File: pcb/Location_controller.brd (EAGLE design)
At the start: 75 x 45 mm, 41 parts, among them IC1 LIS302DL, X1 22-23-2021

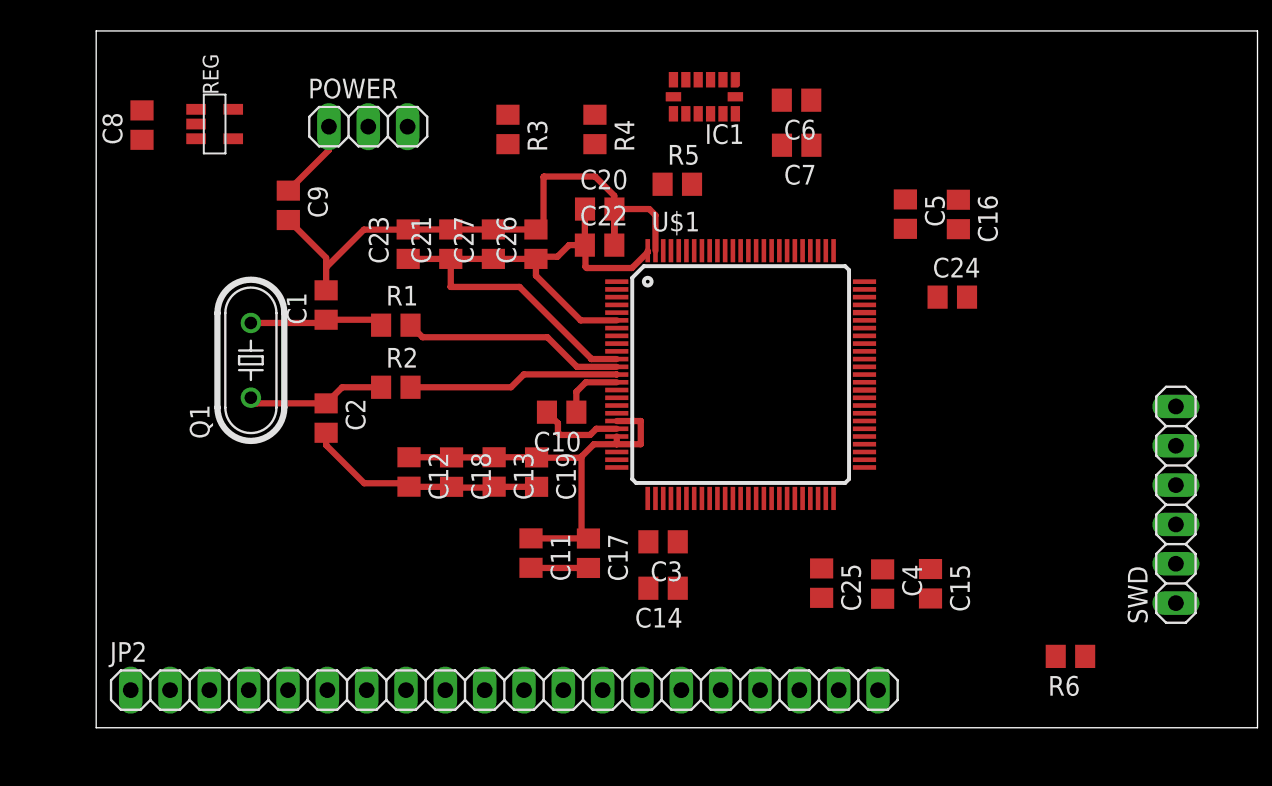
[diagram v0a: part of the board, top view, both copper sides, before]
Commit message: Add more layering
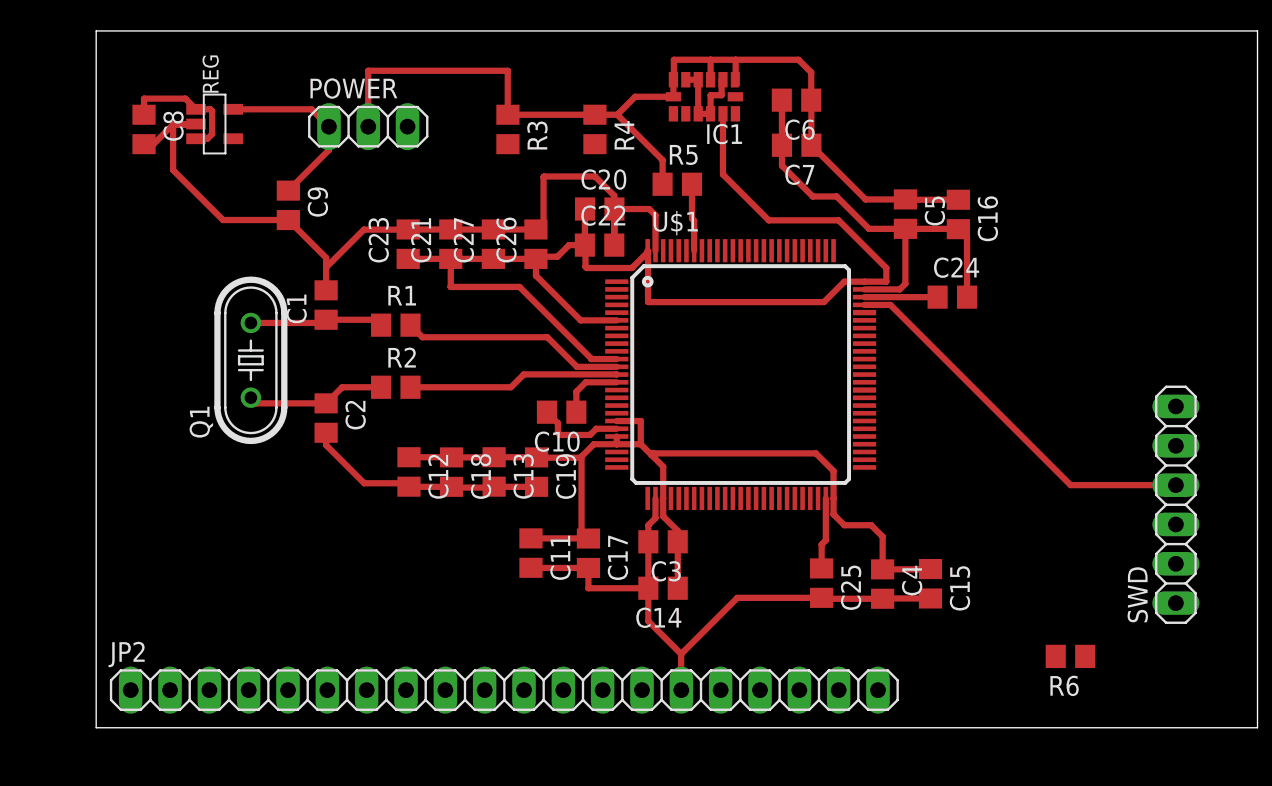
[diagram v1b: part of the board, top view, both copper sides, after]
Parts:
- moved C8 0.31 mm to (3.09, 38.6), turned to 270 degrees
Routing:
- net VDD: track 70.5 -> 204.2 mm
- net GND: track 64.4 -> 152.9 mm
- net SWDIO: track 0.00 -> 24.9 mm
- net N$4: track 0.00 -> 8.43 mm
- net N$10: track 5.22 -> 11.9 mm
- net N$9: track 0.00 -> 4.72 mm
- net N$8: track 0.00 -> 4.63 mm
- net N$3: track 0.00 -> 4.35 mm

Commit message: Further pcb layout routing
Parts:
- added DRN_POWER, RCM_POWER: (no value), pinhead:1X02
- moved C8 52.6 mm to (55.7, 37.7), turned to 90 degrees
- moved C9 52.3 mm to (64.5, 38.7), turned to 0 degrees
- moved REG 51.9 mm to (59.8, 37.8)
- moved POWER 34.4 mm to (51.9, 41.4)
- moved SWD 4.65 mm to (70.7, 9.85)
- moved R6 1.90 mm to (64.8, 4.26)
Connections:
- removed net N$10: C9.1, POWER.1, REG.5
- new net IN_3V: C8.1, POWER.2, REG.1, REG.3
- new net N$5: POWER.1, X1.1
- net GND: now also DRN_POWER.1, RCM_POWER.1
- net N$4: now also DRN_POWER.2, POWER.3; no longer C8.1, REG.1, REG.3, X1.1
- net VDD: now also C9.1, REG.5; no longer POWER.2
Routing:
- net GND: track 152.9 -> 231.7 mm
- net N$4: track 8.43 -> 55.2 mm
- net NRST: track 4.18 -> 44.9 mm, vias 0 -> 2
- net SWO: track 0.00 -> 39.3 mm, vias 0 -> 1
- net SWCLK: track 0.00 -> 37.0 mm, vias 0 -> 1
- net USART2_TX: track 0.00 -> 22.8 mm, vias 0 -> 1
- net USART2_RX: track 0.00 -> 21.3 mm, vias 0 -> 1
- net IN_3V: track 0.00 -> 15.0 mm
- net SWDIO: track 24.9 -> 39.8 mm
- net VDD: track 204.2 -> 216.7 mm
- net N$10: track 11.9 -> 0.00 mm
- net N$6: track 0.00 -> 5.28 mm

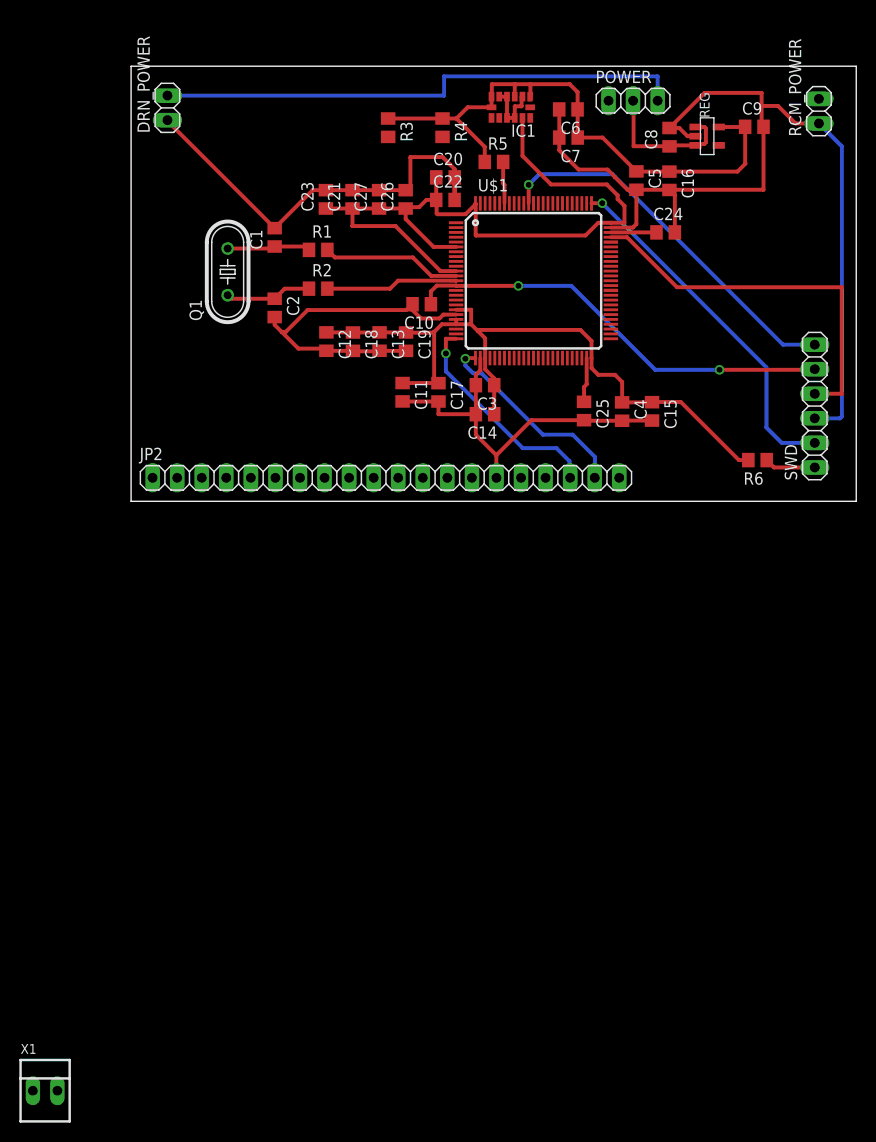
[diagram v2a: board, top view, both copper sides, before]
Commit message: Add barrel DC-jack to pcb
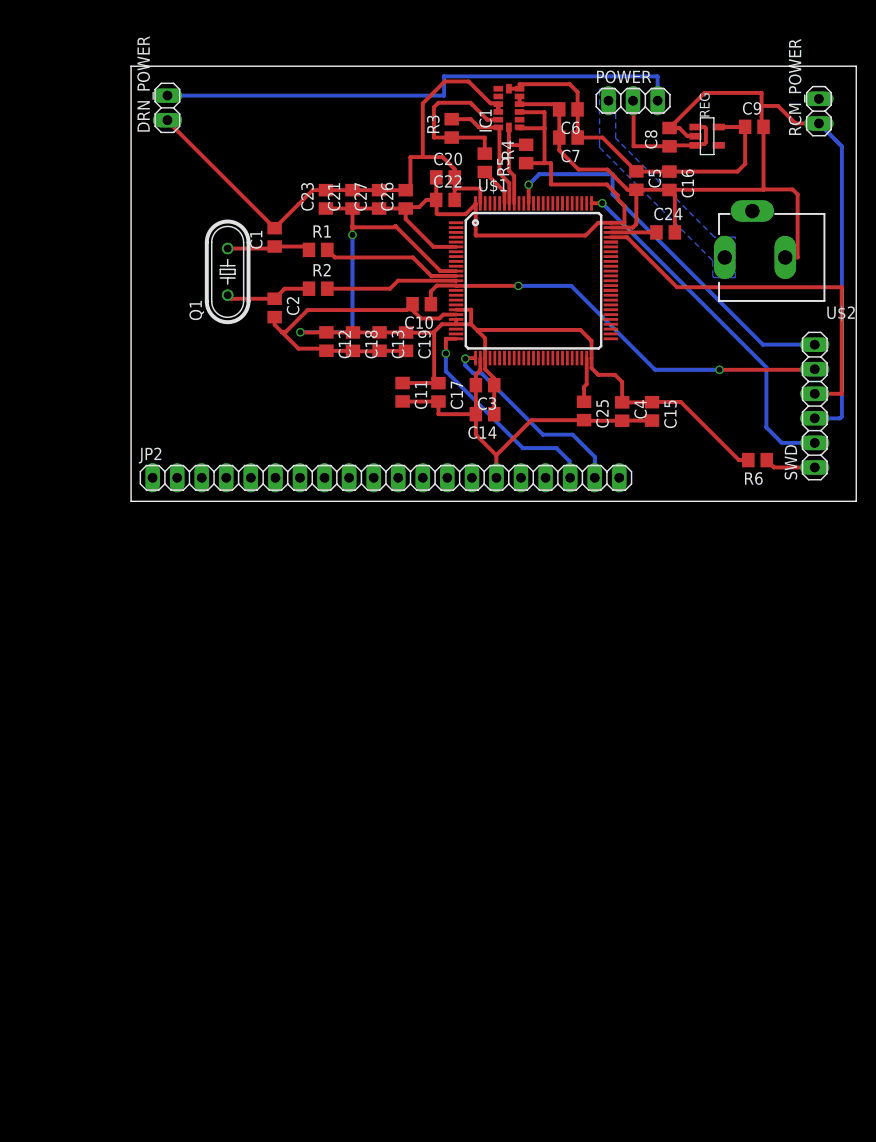
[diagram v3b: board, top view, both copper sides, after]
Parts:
- removed X1: 22-23-2021, con-molex:22-23-2021
- added U$2: DCBARRELPTH, BaseApp:DCJACK_2MM_PTH
- moved R4 9.07 mm to (40.9, 35.9), turned to 90 degrees
- moved R3 6.57 mm to (33.2, 38.6), turned to 90 degrees
- moved R5 0.95 mm to (36.6, 35.0), turned to 270 degrees
- moved IC1 0.22 mm to (39.1, 40.7), turned to 90 degrees
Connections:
- new net GNDBREAK: U$2.GNDBREAK
- net GND: now also U$2.GND; no longer X1.2
- net N$5: now also U$2.PWR; no longer X1.1
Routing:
- net GND: track 231.7 -> 260.7 mm
- net VDD: track 216.7 -> 237.5 mm, vias 0 -> 2
- net I2C_SDA: track 0.00 -> 13.5 mm
- net I2C_SCL: track 0.00 -> 9.89 mm
- net SWO: track 39.3 -> 40.5 mm
- added copper zone on layer 16, net N$5

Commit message: Finish pcb routing
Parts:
- added JP1, JP3: (no value), pinhead:1X06
- JP2: device pinhead:1X20 -> pinhead:1X06
- moved JP2 0.97 mm to (25.4, 2.54)
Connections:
- net GND: now also JP1.1; no longer JP2.15
- net IN_3V: now also RCM_POWER.2
- net USART2_RX: now also JP1.5; no longer JP2.19
- net USART2_TX: now also JP1.4; no longer JP2.18
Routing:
- net GND: track 260.7 -> 324.7 mm, vias 0 -> 6
- net VDD: track 237.5 -> 272.8 mm, vias 2 -> 5
- net IN_3V: track 15.0 -> 39.4 mm
- net N$4: track 55.2 -> 59.9 mm
- net USART2_TX: track 22.8 -> 20.9 mm
- net SWCLK: track 37.0 -> 38.2 mm
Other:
- board size 75 x 45 mm -> 75 x 48 mm

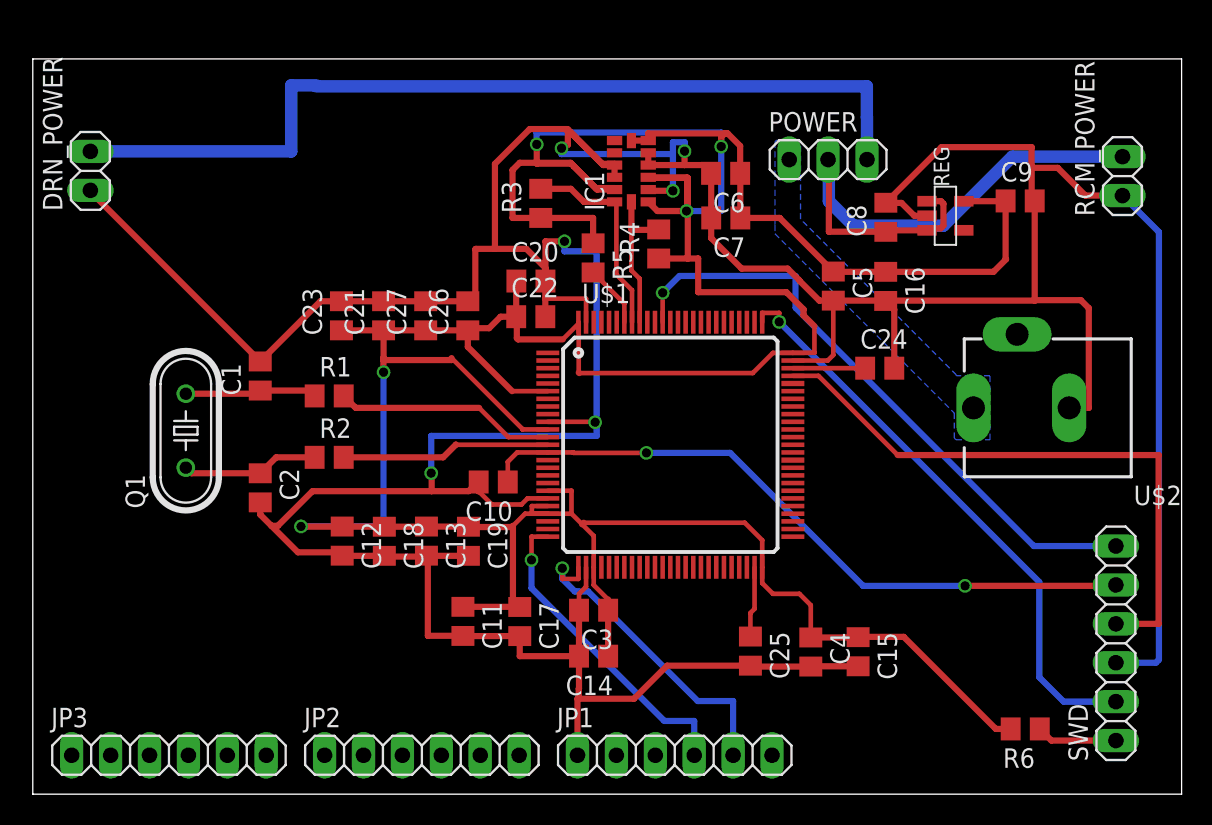
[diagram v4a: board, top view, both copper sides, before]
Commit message: Silk-screening for pcb
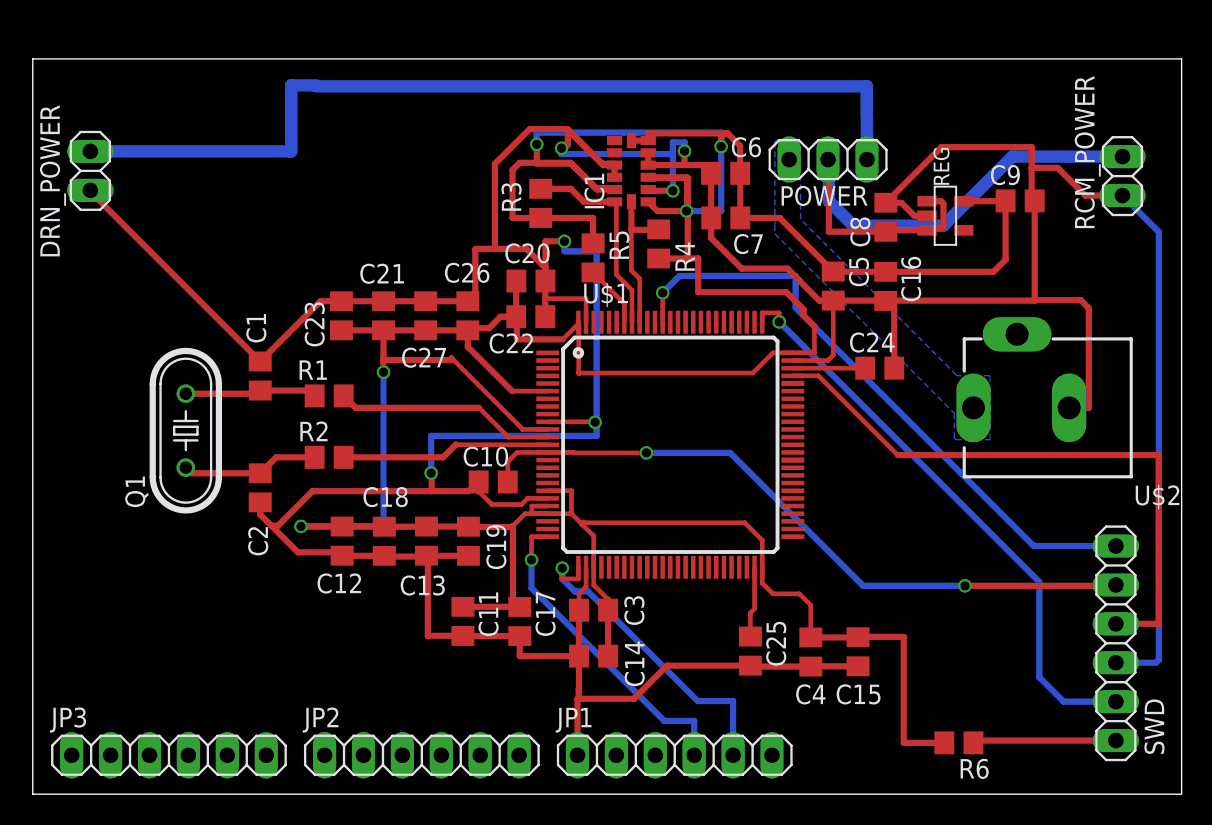
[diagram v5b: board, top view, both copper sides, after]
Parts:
- moved R6 4.42 mm to (60.5, 3.35)
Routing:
- net N$6: track 5.28 -> 9.45 mm
